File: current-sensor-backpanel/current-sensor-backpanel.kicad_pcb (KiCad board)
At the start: 2 copper layers, 98 x 30 mm, 3 parts, among them J1 Conn_01x01_Female, J2 Conn_01x01_Female

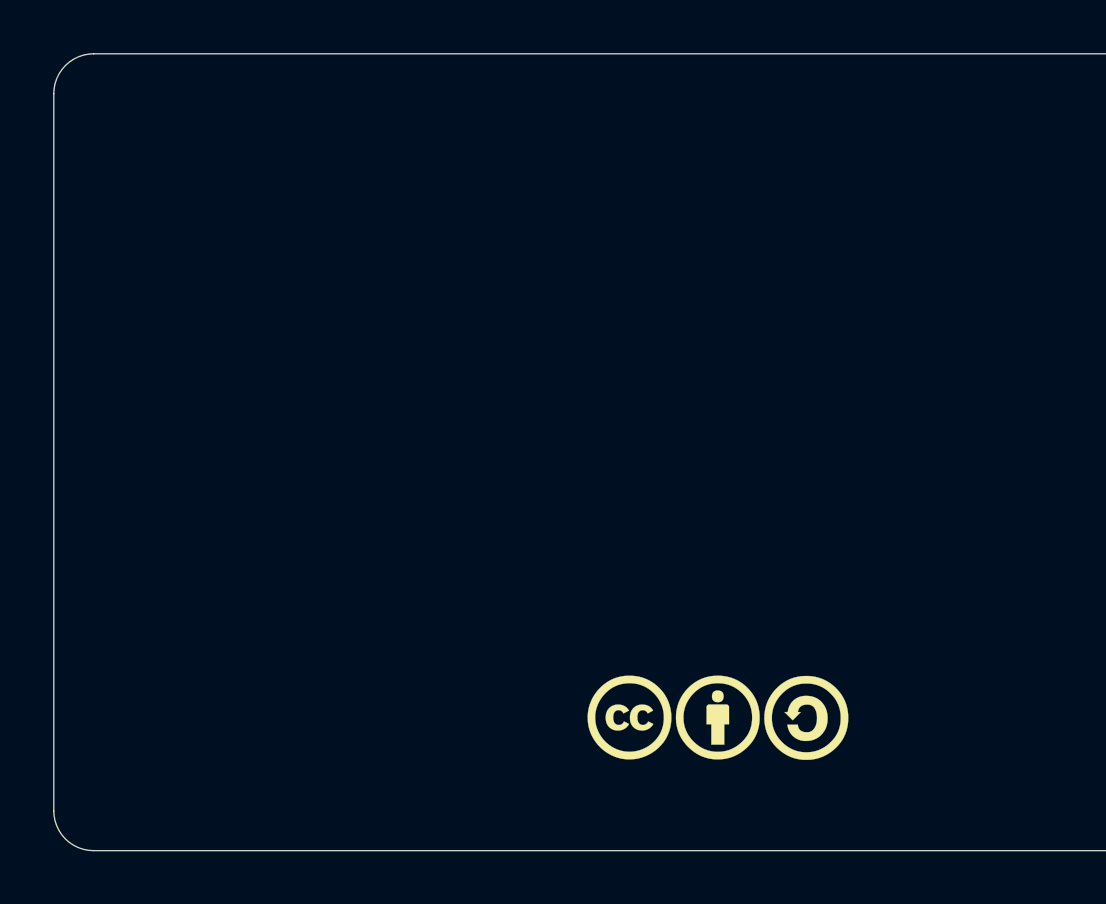
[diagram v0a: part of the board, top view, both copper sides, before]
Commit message: complete mechanical placement of all components on main pcb, and holes on front/back panels
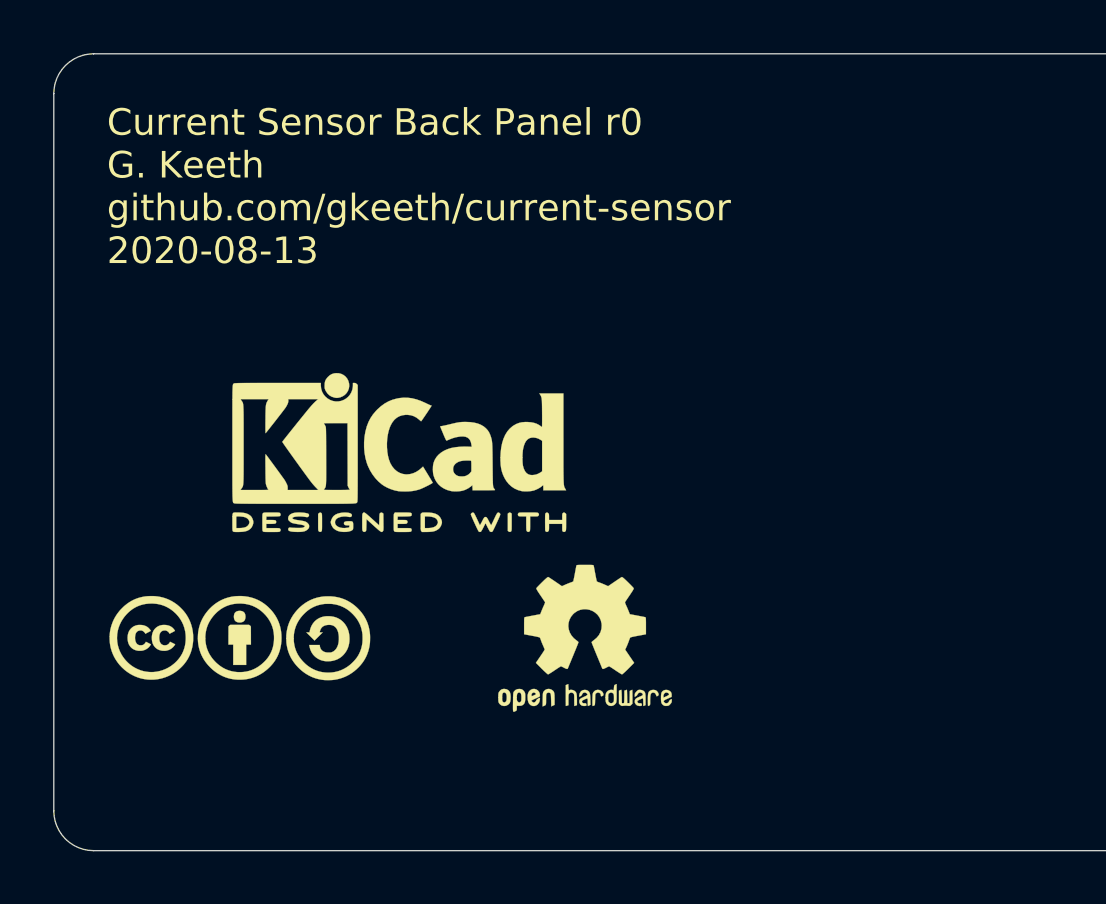
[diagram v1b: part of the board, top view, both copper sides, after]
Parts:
- added LOGO2: Logo_MadeWithKiCad, Symbol:KiCad-Logo2_6mm_SilkScreen, F.Cu at (113.0, 135.0)
- added LOGO3: Logo_Open_Hardware_Small, Symbol:OSHW-Logo2_7.3x6mm_SilkScreen, F.Cu at (120.0, 142.0)
- moved LOGO1 18.2 mm to (107.0, 142.0)
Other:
- board text added: "Current Sensor Back Panel r0 G. Keeth github.com/gkeeth/current-sensor 2020-08-13"

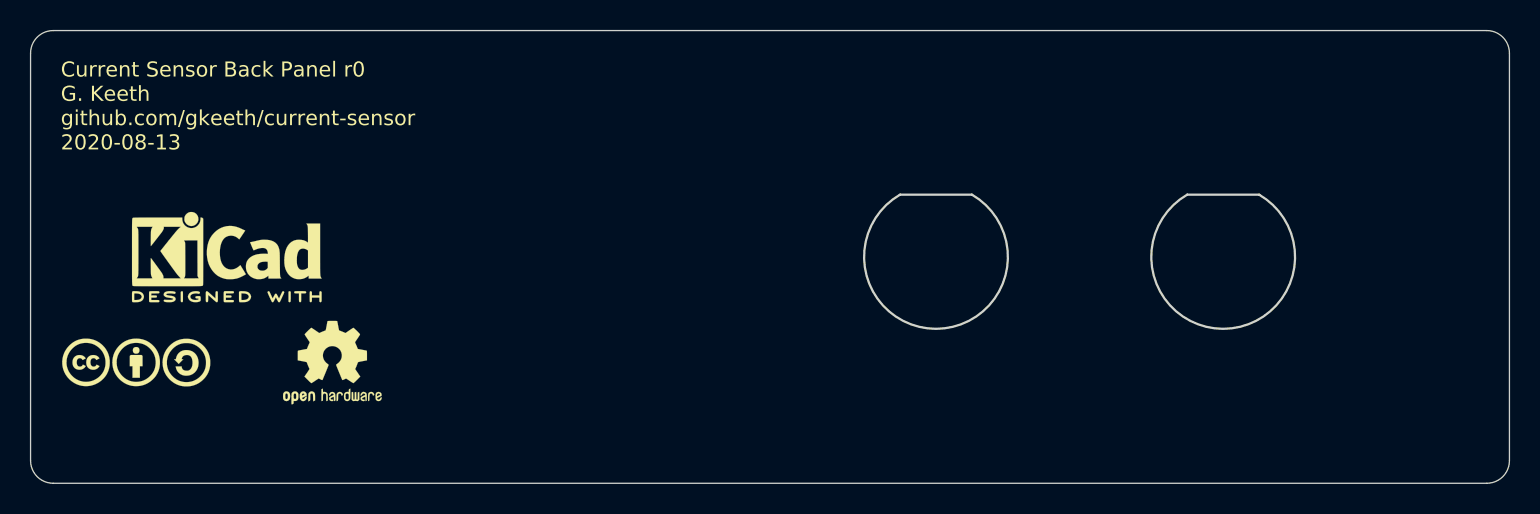
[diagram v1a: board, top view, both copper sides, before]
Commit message: add back panel label
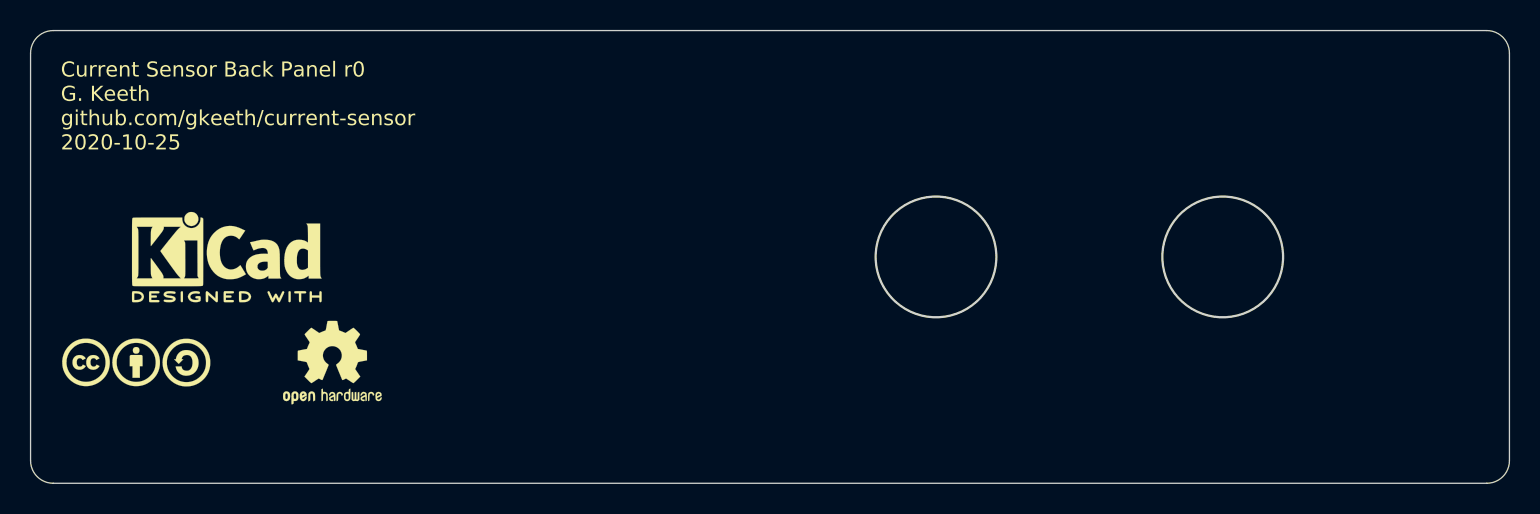
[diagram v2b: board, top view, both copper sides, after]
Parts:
- removed J1, J2: Conn_01x01_Female, Panel_Cutouts:BindingPost_Pomona_3750_3760_3770
- added C1: CalTest_CT2232-4, Panel_Cutouts:Panel_BindingPost_CalTest_CT2232-x, B.Cu at (160.0, 135.0)
- added C2: CalTest_CT2232-4, Panel_Cutouts:Panel_BindingPost_CalTest_CT2232-x, B.Cu at (179.0, 135.0)
- added C3: Front Panel Label, current-sensor:backpanel, B.Cu at (179.0, 135.0)
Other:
- board text added: "Current Sensor Back Panel r0 G. Keeth github.com/gkeeth/current-sensor 2020-10-25"
- board text removed: "Current Sensor Back Panel r0 G. Keeth github.com/gkeeth/current-sensor 2020-08-13"
